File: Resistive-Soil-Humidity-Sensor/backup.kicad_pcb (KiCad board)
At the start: 2 copper layers, 8 parts, among them Q1 BC547

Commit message: add pcb-layout
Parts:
- +9V1: moved to F.Cu
- H1: value sensor -> MountingHole
- H2: value MountingHole_Pad -> MountingHole
- moved D1 152.2 mm to (114.6, 29.1)
- moved RV1 152.2 mm to (105.2, 28.8)
- moved R1 152.2 mm to (106.1, 25.3)
- moved Q1 152.2 mm to (123.6, 30.7)
- moved Voltage-Reg1 152.2 mm to (98.5, 30.4)
- moved H1 150.7 mm to (133.9, 31.8)
- moved H2 150.7 mm to (133.9, 29.5)
- moved +9V1 127.5 mm to (104.2, 52.2)
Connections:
- H1 pad 1: Net-(H1-Pad1) -> (no net)
- H2 pad 1: Net-(BZ1-Pad1) -> (no net)
- Q1 pad 2: Net-(H1-Pad1) -> Net-(Q1-Pad2)
- RV1 pad 2: Net-(H1-Pad1) -> Net-(Q1-Pad2)
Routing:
- net Net-(H1-Pad1): track 33.8 -> 0.00 mm
- net Net-(Q1-Pad2): track 0.00 -> 27.3 mm
- net Net-(+9V1-Pad2): track 42.1 -> 27.8 mm
- net Net-(+9V1-Pad1): track 6.57 -> 0.00 mm
- net Net-(BZ1-Pad1): track 45.5 -> 42.7 mm

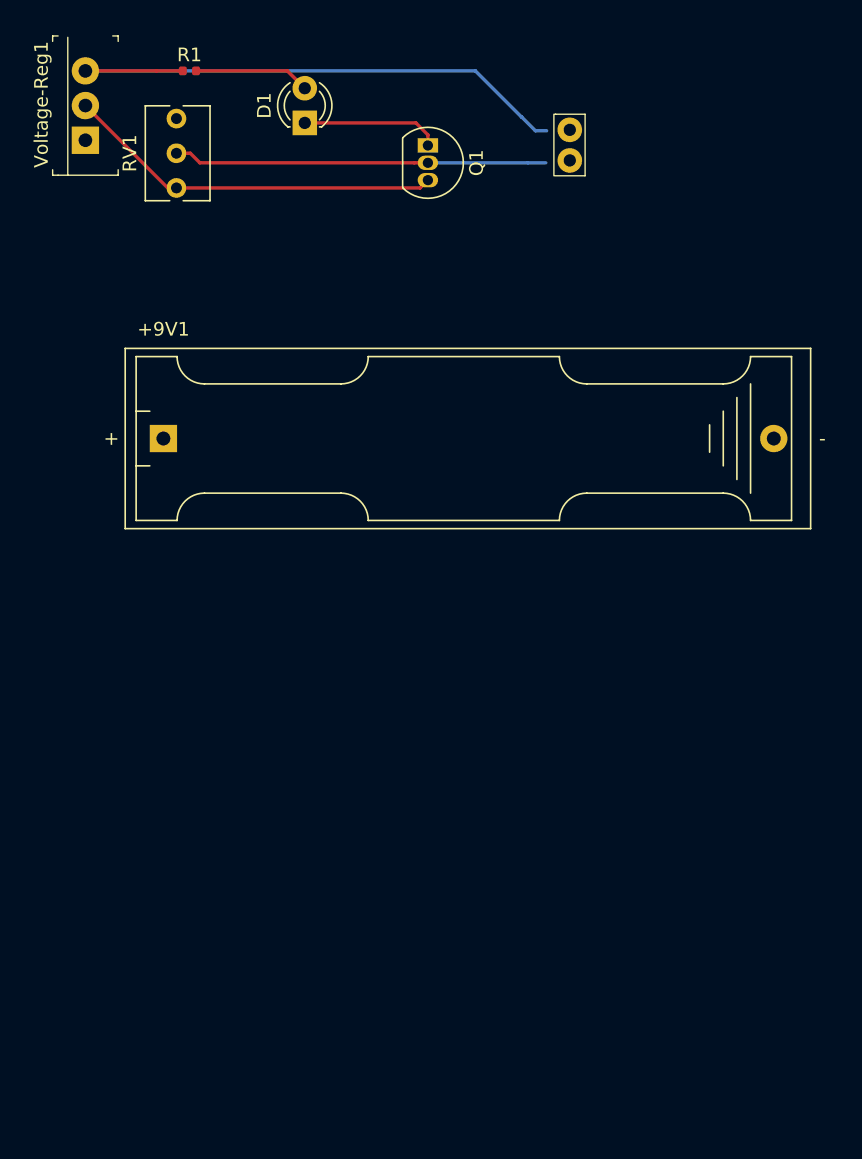
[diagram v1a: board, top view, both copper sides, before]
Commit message: update footprints & recover design
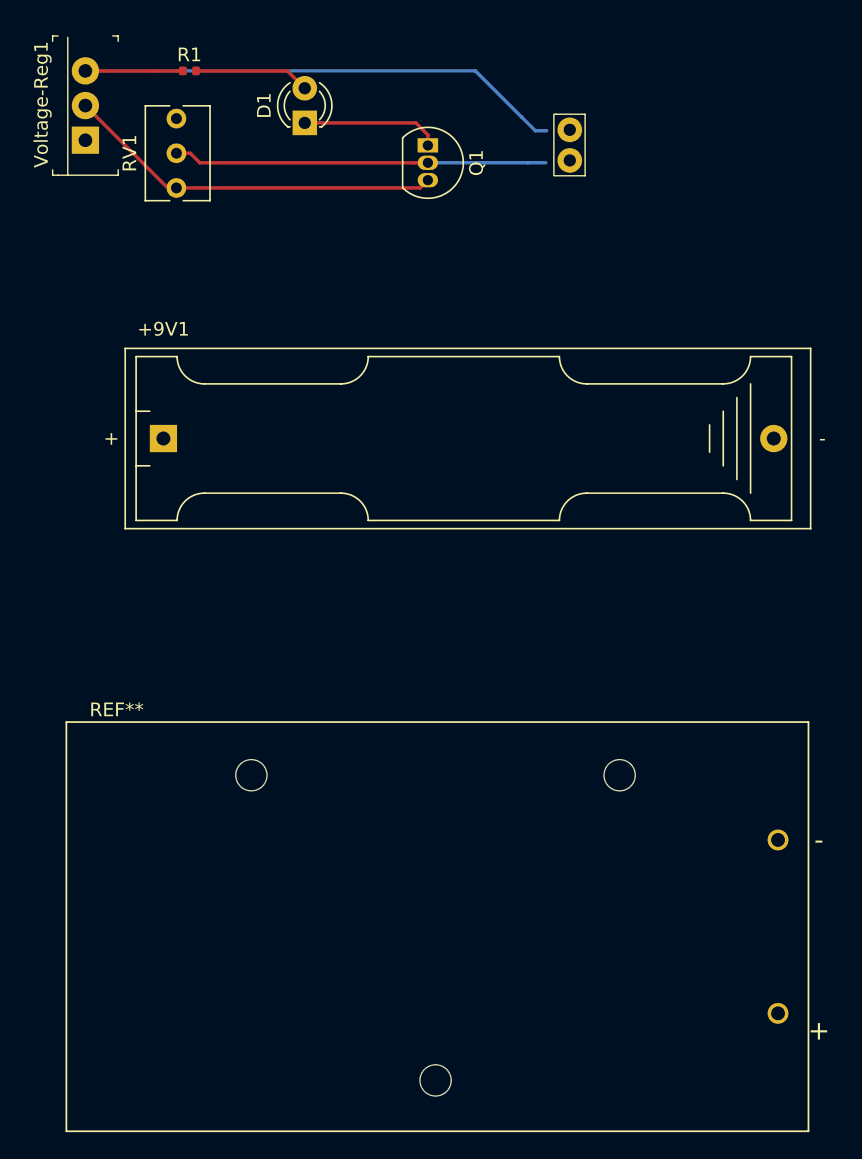
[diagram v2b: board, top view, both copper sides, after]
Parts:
- added REF**: BAT_BH9VPC, BHVPC-BatteryHolder:BAT_BH9VPC, F.Cu at (124.3, 87.9)
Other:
- net class Default removed
